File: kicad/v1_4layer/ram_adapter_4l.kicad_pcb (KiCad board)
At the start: 4 copper layers, 18.3 x 41.1 mm, 5 parts, among them J1 Conn_01x16_Male, J2 Conn_01x16_Male, U1 IS61C5128AL-10KLI

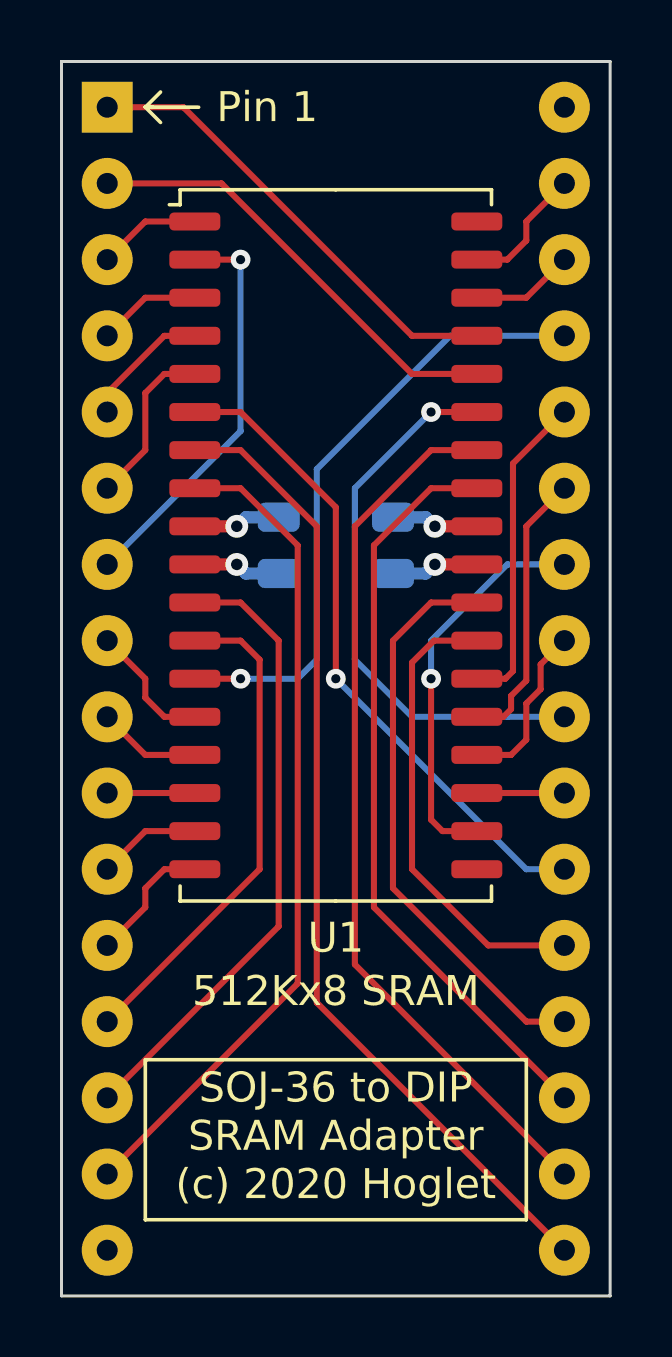
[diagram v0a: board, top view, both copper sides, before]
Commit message: Updated silk screen
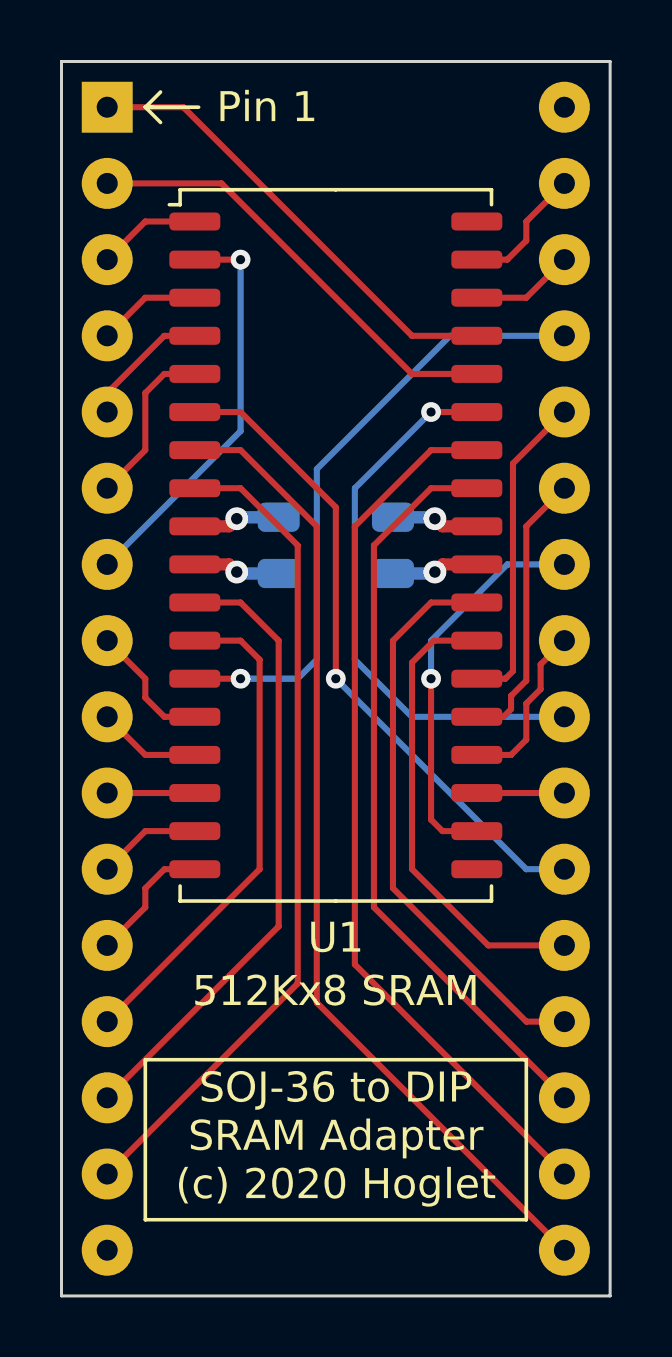
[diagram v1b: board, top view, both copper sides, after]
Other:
- rule pad_to_mask_clearance: 0 -> 0.1

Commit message: Extended SOJ pads by 0.2mm
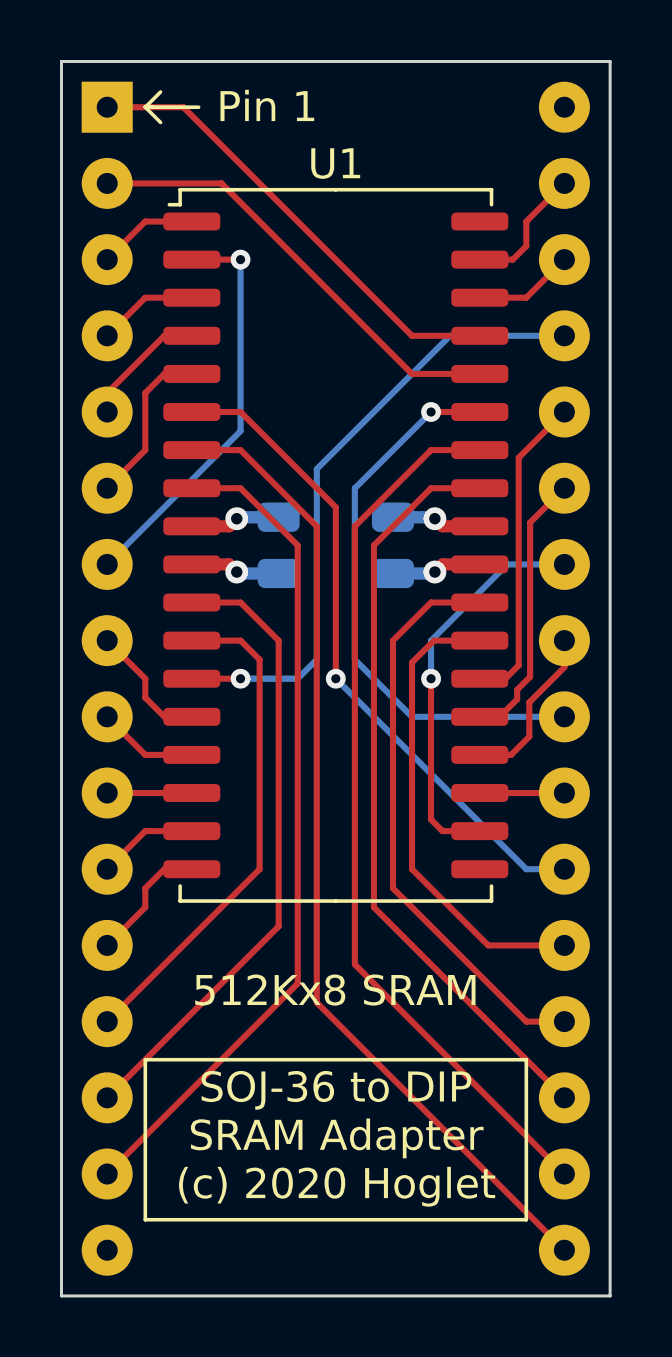
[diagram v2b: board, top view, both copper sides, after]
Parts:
- U1: footprint Package_SO:SOJ-36_10.16x23.49mm_P1.27mm -> footprints:SOJ-36_10.16x23.49mm_P1.27mm
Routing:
- net /A13: track 11.0 -> 10.3 mm
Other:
- net class Default: clearance 0.2032 -> 0.1778
- rule trace_clearance: 0.2032 -> 0.1778

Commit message: Tweak thermals
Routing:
- net /VCC: track 5.84 -> 15.6 mm
- net /GND: track 5.84 -> 15.6 mm

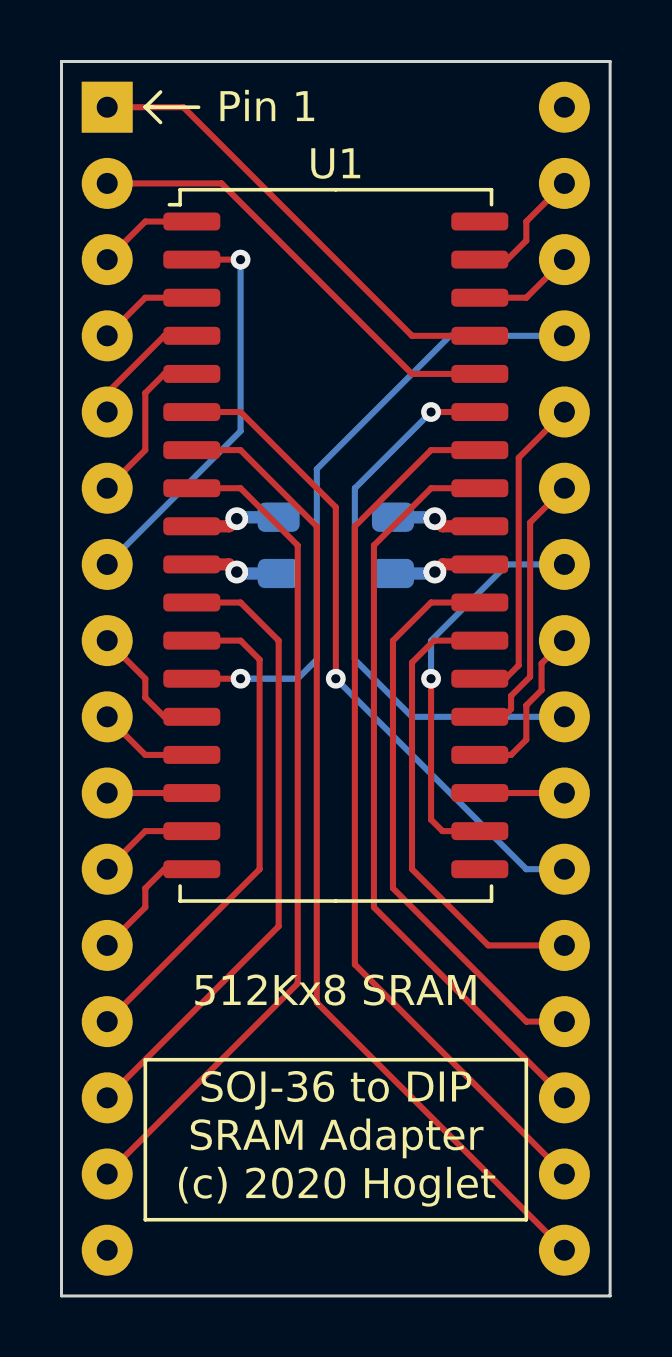
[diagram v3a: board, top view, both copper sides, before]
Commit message: Added ground points
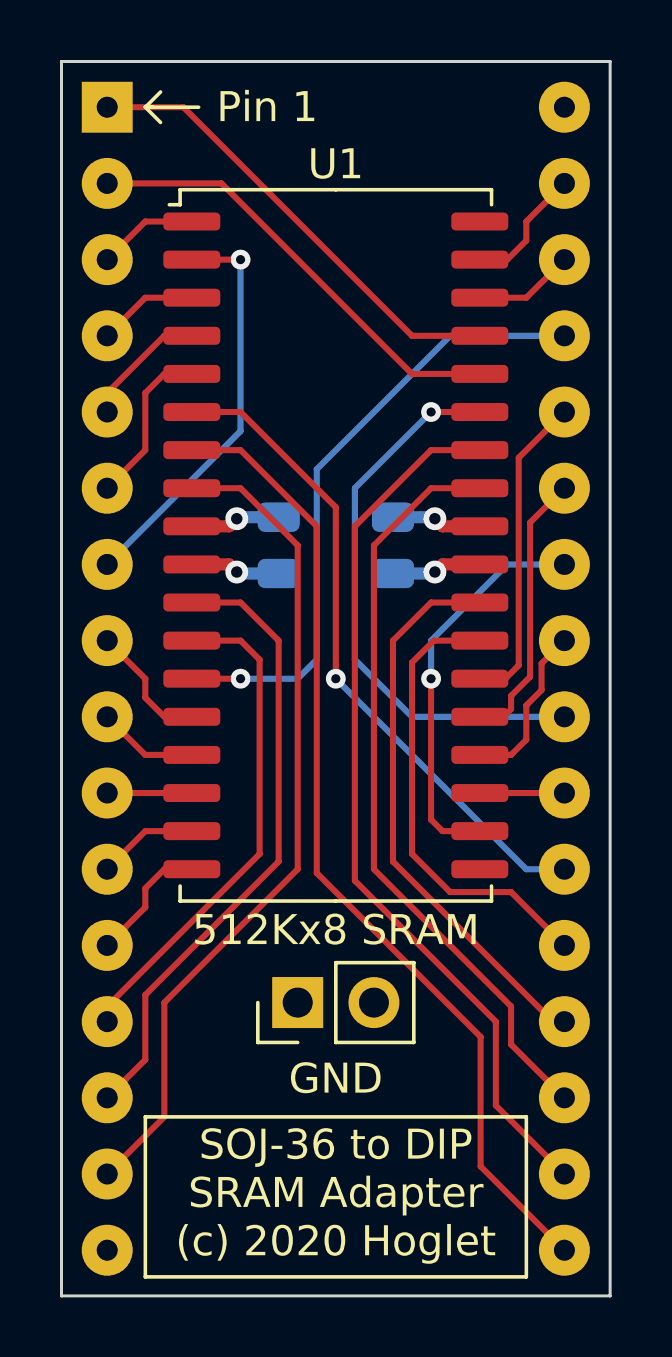
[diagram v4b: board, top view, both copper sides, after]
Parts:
- added J3: Conn_01x02_Male, Connector_PinHeader_2.54mm:PinHeader_1x02_P2.54mm_Vertical, F.Cu at (95.2, 95.9)
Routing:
- net /DQ6: track 19.1 -> 18.6 mm
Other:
- board text added: "GND"
